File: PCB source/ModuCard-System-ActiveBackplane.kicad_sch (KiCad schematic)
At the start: 8 parts

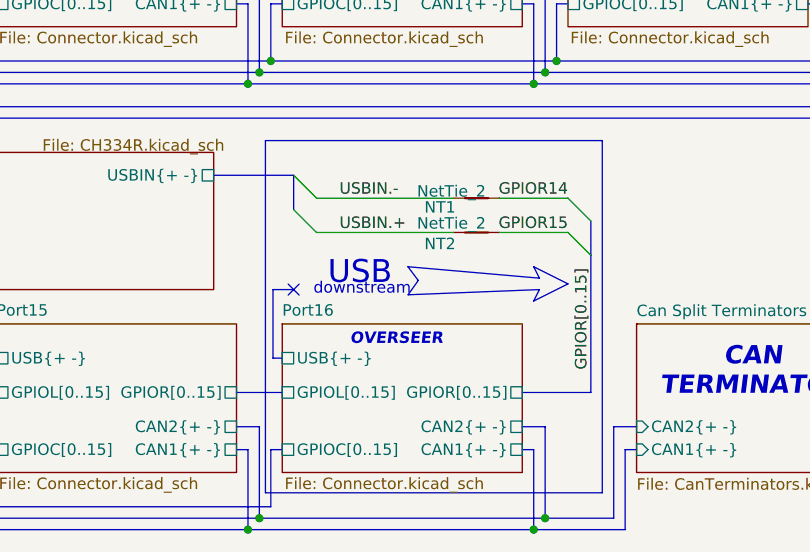
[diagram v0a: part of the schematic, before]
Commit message: change USB upstream pinout
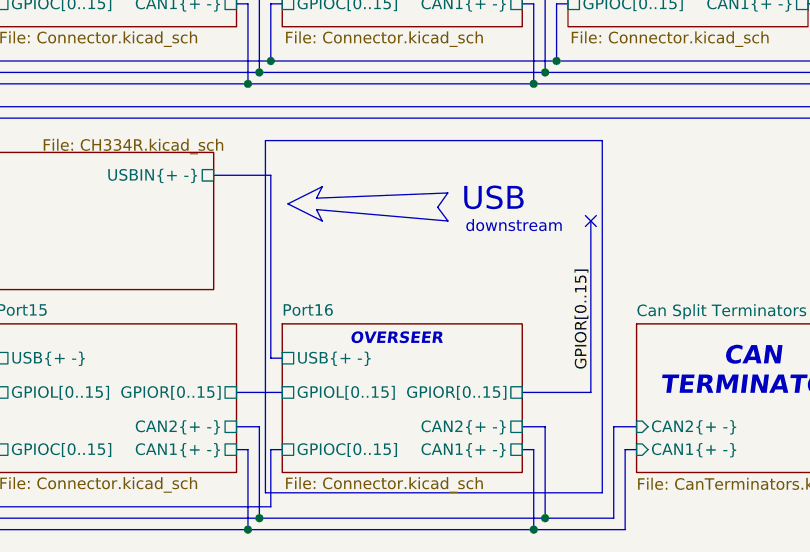
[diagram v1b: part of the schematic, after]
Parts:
- removed NT1, NT2: NetTie_2, NetTie:NetTie-2_SMD_Pad0.5mm, symbol Device:NetTie_2
